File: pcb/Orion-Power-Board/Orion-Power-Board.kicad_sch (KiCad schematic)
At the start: 12 parts, among them M1 Motor_Servo, M10 Motor_Servo, M11 Motor_Servo, M12 Motor_Servo, M2 Motor_Servo, M3 Motor_Servo, M4 Motor_Servo, M5 Motor_Servo, M6 Motor_Servo, M7 Motor_Servo, M8 Motor_Servo, M9 Motor_Servo

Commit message: Power board
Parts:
- added BT1, BT2: LI-ION 7.4V 3000 mAh, AA_Custom_Components:PowerPad_Pair_5.0x5.0mm_1PadFlipped, symbol Device:Battery_Cell
- added C1, C2, C3, C4: 470uF_CAP, symbol Device:C_Polarized_US
- added C5, C6, C7, C8: 470uF_CAP, Capacitor_THT:CP_Radial_D8.0mm_P3.50mm, symbol Device:C_Polarized_US
- added H1, H2, H3, H4: MountingHole, MountingHole:MountingHole_3.2mm_M3_Pad, symbol Mechanical:MountingHole
- added J1: Keyed Connector 20 pos, AA_Custom_Components:SULLINS_SFH11-PBPC-D10-ST-BK, symbol AA_Custom_Components:20PosKeyedMale
- added J2, J3: 2S_BATTERY_BALANCE_HEADER, AA_Custom_Components:JST_XH_1x03_P2.54mm_Vertical, symbol AA_Custom_Components:2S_BATTERY_BALANCE_HEADER
- added J4: 3S_BATTERY_BALANCE_HEADER, AA_Custom_Components:JST_XH_1x04_P2.54mm_Vertical, symbol AA_Custom_Components:3S_BATTERY_BALANCE_HEADER
- added N1, N2, N4: CENTER_POS, AA_Custom_Components:Polarity_Center_Positive_7.5mm_SilkScreen, symbol Mechanical:Housing
- added N3: KiCad, Symbol:KiCad-Logo2_8mm_SilkScreen, symbol Mechanical:Housing
- added U1, U2: 6x3_SERVO_HEADER_PIN, AA_Custom_Components:PinHeader_3x06_P2.54mm_Vertical, symbol AA_Custom_Components:6x3_SERVO_HEADER_PIN
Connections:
- net +7.4V_BACK_BATT: now also BT2.1 (+), C3.1, C4.1, C7.2, C8.2, U1.1 (7.4V), U1.2 (7.4V), U1.3 (7.4V), U1.4 (7.4V), U1.5 (7.4V), U1.6 (7.4V)
- net +7.4V_FRONT_BATT: now also BT1.1 (+), C1.1, C2.1, C5.2, C6.2, U2.1 (7.4V), U2.2 (7.4V), U2.3 (7.4V), U2.4 (7.4V), U2.5 (7.4V), U2.6 (7.4V)
- net GND: now also BT1.2 (-), BT2.2 (-), C1.2, C2.2, C3.2, C4.2, C5.1, C6.1, C7.1, C8.1, J1.19, J2.3 (GND), J3.3 (GND), J4.4 (GND), U1.10 (GND), U1.11 (GND), U1.12 (GND), U1.7 (GND), U1.8 (GND), U1.9 (GND), U2.10 (GND), U2.11 (GND), U2.12 (GND), U2.7 (GND), U2.8 (GND), U2.9 (GND); no longer M9.3 (-)
- net SERVO_01: no longer names the net of M1.1 (PWM)
- net SERVO_02: no longer names the net of M3.1 (PWM)
- net SERVO_03 renamed PWM2
- net PWM2: now also J1.3, U2.16 (OUT3)
- net SERVO_04 renamed PWM3
- net PWM3: now also J1.4, U2.15 (OUT4)
- net SERVO_05 renamed PWM4
- net PWM4: now also J1.5, U2.14 (OUT5)
- net SERVO_06 renamed PWM5
- net PWM5: now also J1.6, U2.13 (OUT6)
- net SERVO_07 renamed PWM6
- net PWM6: now also J1.7, U1.18 (OUT1)
- net SERVO_08 renamed PWM7
- net PWM7: now also J1.8, U1.17 (OUT2)
- net SERVO_09 renamed PWM8
- net PWM8: now also J1.9, U1.16 (OUT3)
- net SERVO_10 renamed PWM9
- net PWM9: now also J1.10, U1.15 (OUT4)
- net SERVO_11 renamed PWM10
- net PWM10: now also J1.11, U1.14 (OUT5)
- net SERVO_12 renamed PWM11
- net PWM11: now also J1.12, U1.13 (OUT6)
- new net 2S_BACK_BATT_CELL1: J1.14, J3.1 (C1)
- new net 2S_BACK_BATT_CELL2: J1.16, J3.2 (C2)
- new net 2S_FRONT_BATT_CELL1: J1.18, J2.1 (C1)
- new net 2S_FRONT_BATT_CELL2: J1.20, J2.2 (C2)
- new net 3S_BATT_CELL1: J1.13, J4.1 (C1)
- new net 3S_BATT_CELL2: J1.15, J4.2 (C2)
- new net 3S_BATT_CELL3: J1.17, J4.3 (C3)
- new net PWM0: J1.1, U2.18 (OUT1)
- new net PWM1: J1.2, U2.17 (OUT2)
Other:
- note added: "MOUNTING HARDWARE"
- note added: "ORION POWER BOARD"
- note added: "PCB LOGOS"
- moved on the sheet: M1, M10, M11, M12, M2, M3, M4, M5, M6, M7, M8, M9

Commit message: Done layout of power board
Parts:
- removed C1, C2, C3, C4: 470uF_CAP, symbol Device:C_Polarized_US
- removed J1: Keyed Connector 20 pos, AA_Custom_Components:SULLINS_SFH11-PBPC-D10-ST-BK, symbol AA_Custom_Components:20PosKeyedMale
- removed M1, M10, M11, M12, M2, M3, M4, M5, M6, M7, M8, M9: Motor_Servo, symbol Motor:Motor_Servo
- removed N2, N4: CENTER_POS, AA_Custom_Components:Polarity_Center_Positive_7.5mm_SilkScreen, symbol Mechanical:Housing
- removed N3: KiCad, Symbol:KiCad-Logo2_8mm_SilkScreen, symbol Mechanical:Housing
- added J5: 3S_LI-ION_VOLTAGE_ALARM, AA_Custom_Components:LIPO_VOLTAGE_ALARM, symbol AA_Custom_Components:LIPO_VOLTAGE_ALARM
- added J6: 2S_BACK_LI-ION_VOLTAGE_ALARM, AA_Custom_Components:LIPO_VOLTAGE_ALARM, symbol AA_Custom_Components:LIPO_VOLTAGE_ALARM
- added J7: 2S_FRONT_LI-ION_VOLTAGE_ALARM, AA_Custom_Components:LIPO_VOLTAGE_ALARM, symbol AA_Custom_Components:LIPO_VOLTAGE_ALARM
- added J8: CONN_20_POS_KEYED_SOCKET, AA_Custom_Components:SULLINS_SBH11-PBPC-D10-ST-BK_SOCKET, symbol AA_Custom_Components:CONN_20_POS_KEYED_SOCKET
- BT1: value LI-ION 7.4V 3000 mAh -> 2S_FRONT_LI-ION_BATT; footprint AA_Custom_Components:PowerPad_Pair_5.0x5.0mm_1PadFlipped -> AA_Custom_Components:PowerPad_Pair_5.0x5.0mm_2ndPadFlipped
- BT2: value LI-ION 7.4V 3000 mAh -> 2S_BACK_LI-ION_BATT; footprint AA_Custom_Components:PowerPad_Pair_5.0x5.0mm_1PadFlipped -> AA_Custom_Components:PowerPad_Pair_5.0x5.0mm_2ndPadFlipped
- J2: value 2S_BATTERY_BALANCE_HEADER -> 2S_FRONT_BATTERY_BALANCE_HEADER
- J3: value 2S_BATTERY_BALANCE_HEADER -> 2S_BACK_BATTERY_BALANCE_HEADER
- U1: value 6x3_SERVO_HEADER_PIN -> BACK_6x3_SERVO_HEADER_PIN; footprint AA_Custom_Components:PinHeader_3x06_P2.54mm_Vertical -> AA_Custom_Components:Servo_PinHeader_3x06_P2.54mm_Vertical
- U2: value 6x3_SERVO_HEADER_PIN -> FRONT_6x3_SERVO_HEADER_PIN; footprint AA_Custom_Components:PinHeader_3x06_P2.54mm_Vertical -> AA_Custom_Components:Servo_PinHeader_3x06_P2.54mm_Vertical
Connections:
- net +7.4V_BACK_BATT: now also U1.10 (7.4V), U1.11 (7.4V), U1.12 (7.4V), U1.7 (7.4V), U1.8 (7.4V), U1.9 (7.4V); no longer U1.1 (7.4V), U1.2 (7.4V), U1.3 (7.4V), U1.4 (7.4V), U1.5 (7.4V), U1.6 (7.4V)
- net +7.4V_FRONT_BATT: now also U2.10 (7.4V), U2.11 (7.4V), U2.12 (7.4V), U2.7 (7.4V), U2.8 (7.4V), U2.9 (7.4V); no longer U2.1 (7.4V), U2.2 (7.4V), U2.3 (7.4V), U2.4 (7.4V), U2.5 (7.4V), U2.6 (7.4V)
- net 3S_BATT_CELL1: now also J5.2 (1S), J8.13
- net 3S_BATT_CELL2: now also J5.3 (2S), J8.15
- net 3S_BATT_CELL3: now also J5.4 (3S), J8.17
- net GND: now also U1.13 (GND), U1.14 (GND), U1.15 (GND), U1.16 (GND), U1.17 (GND), U1.18 (GND), U2.13 (GND), U2.14 (GND), U2.15 (GND), U2.16 (GND), U2.17 (GND), U2.18 (GND), J5.1 (GND), J6.1 (GND), J7.1 (GND), J8.19; no longer U1.10 (GND), U1.11 (GND), U1.12 (GND), U1.7 (GND), U1.8 (GND), U1.9 (GND), U2.10 (GND), U2.11 (GND), U2.12 (GND), U2.7 (GND), U2.8 (GND), U2.9 (GND)
- net PWM0: now also U2.1 (PWM0), J8.1; no longer U2.18 (OUT1)
- net PWM1: now also U2.2 (PWM1), J8.2; no longer U2.17 (OUT2)
- net PWM10: now also U1.5 (PWM4), J8.11; no longer U1.14 (OUT5)
- net PWM11: now also U1.6 (PWM5), J8.12; no longer U1.13 (OUT6)
- net PWM2: now also U2.3 (PWM2), J8.3; no longer U2.16 (OUT3)
- net PWM3: now also U2.4 (PWM3), J8.4; no longer U2.15 (OUT4)
- net PWM4: now also U2.5 (PWM4), J8.5; no longer U2.14 (OUT5)
- net PWM5: now also U2.6 (PWM5), J8.6; no longer U2.13 (OUT6)
- net PWM6: now also U1.1 (PWM0), J8.7; no longer U1.18 (OUT1)
- net PWM7: now also U1.2 (PWM1), J8.8; no longer U1.17 (OUT2)
- net PWM8: now also U1.3 (PWM2), J8.9; no longer U1.16 (OUT3)
- net PWM9: now also U1.4 (PWM3), J8.10; no longer U1.15 (OUT4)
- net 2S_BACK_BATT_CELL1 renamed 2S_BATT_REAR_CELL1
- net 2S_BATT_REAR_CELL1: now also J6.2 (1S), J8.14
- net 2S_BACK_BATT_CELL2 renamed 2S_BATT_REAR_CELL2
- net 2S_BATT_REAR_CELL2: now also J6.3 (2S), J8.16
- net 2S_FRONT_BATT_CELL1 renamed 2S_BATT_FRONT_CELL1
- net 2S_BATT_FRONT_CELL1: now also J7.2 (1S), J8.18
- net 2S_FRONT_BATT_CELL2 renamed 2S_BATT_FRONT_CELL2
- net 2S_BATT_FRONT_CELL2: now also J7.3 (2S), J8.20
- no-connect marks 0 -> 17
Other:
- moved on the sheet: BT1, BT2, C5, C6, C7, C8, N1

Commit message: Update power board
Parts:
- N1: value CENTER_POS -> ORION_LOGO; footprint AA_Custom_Components:Polarity_Center_Positive_7.5mm_SilkScreen -> Orion-Logo:Orion-Logo-20mm
- renumbered C6 to C1, C7 to C2, C5 to C3, C8 to C4, J2 to J1, J3 to J2, J4 to J3, J8 to J4, J7 to J5, J5 to J7, U2 to U1, U1 to U2
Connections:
- net 2S_BATT_FRONT_CELL1: now also J4.16; no longer J4.18
- net 2S_BATT_FRONT_CELL2: now also J4.14; no longer J4.20
- net 2S_BATT_REAR_CELL1: now also J4.20; no longer J4.14
- net 2S_BATT_REAR_CELL2: now also J4.18; no longer J4.16
- net 3S_BATT_CELL1: now also J4.17; no longer J4.13
- net 3S_BATT_CELL3: now also J4.13; no longer J4.17

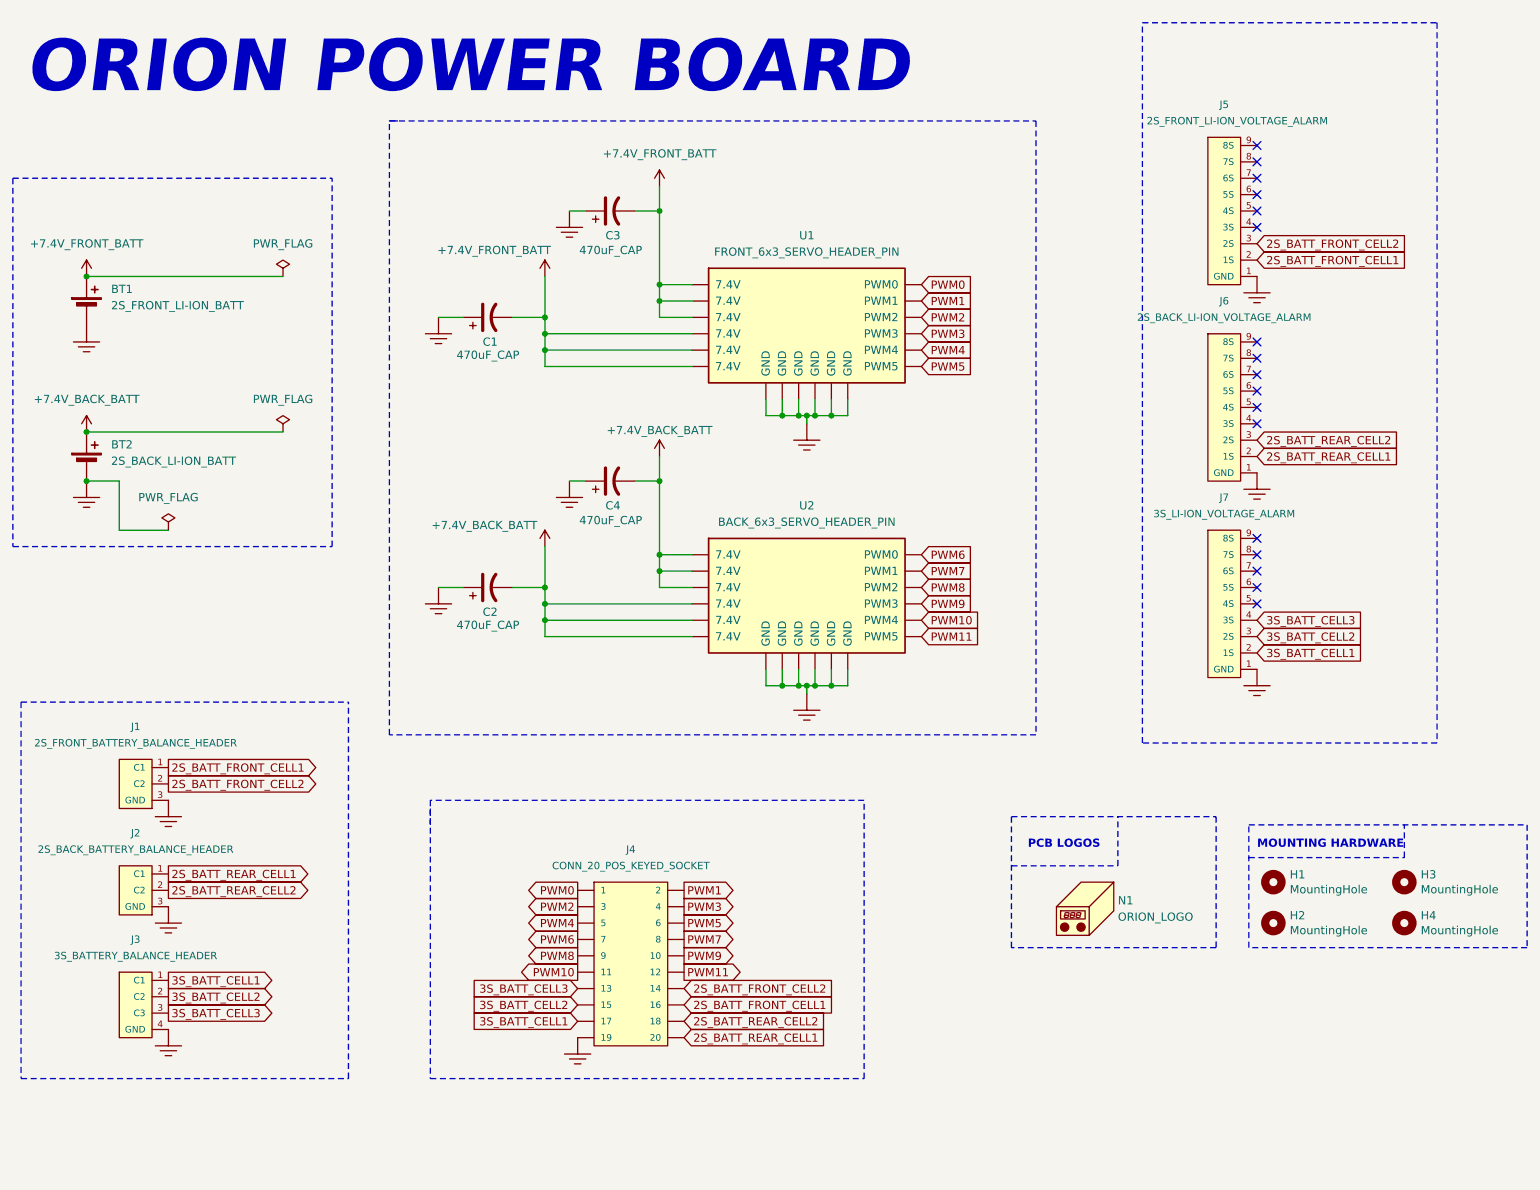
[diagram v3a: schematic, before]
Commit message: Almost finished power board
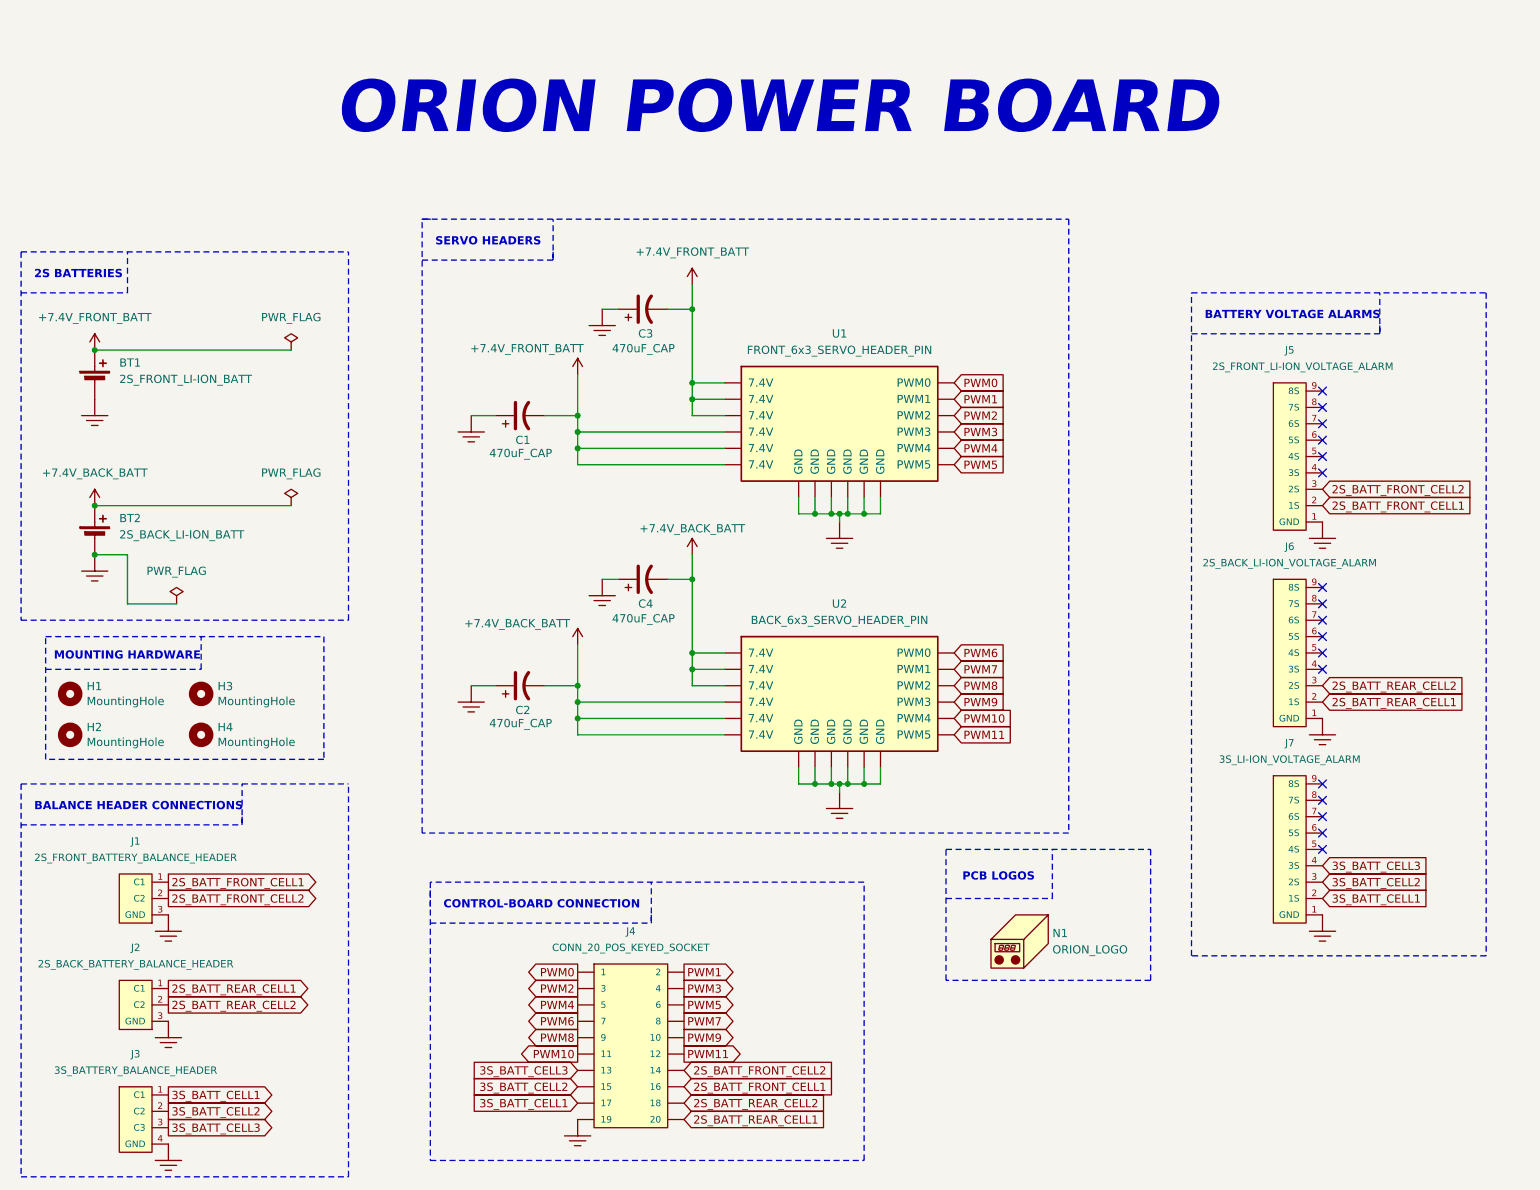
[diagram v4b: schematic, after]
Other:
- note added: "2S BATTERIES"
- note added: "BALANCE HEADER CONNECTIONS"
- note added: "BATTERY VOLTAGE ALARMS"
- note added: "CONTROL-BOARD CONNECTION"
- note added: "SERVO HEADERS"
- moved on the sheet: BT1, BT2, C1, C2, C3, C4, H1, H2, H3, H4, J1, J2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

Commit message: Finished power board
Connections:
- net +7.4V_FRONT_BATT: now also C1.1, C3.1; no longer C1.2, C3.2
- net 2S_BATT_FRONT_CELL1: now also J1.2 (C1); no longer J1.1 (C1)
- net 2S_BATT_FRONT_CELL2: now also J1.1 (C2); no longer J1.2 (C2)
- net 2S_BATT_REAR_CELL1: now also J2.2 (C1); no longer J2.1 (C1)
- net 2S_BATT_REAR_CELL2: now also J2.1 (C2); no longer J2.2 (C2)
- net 3S_BATT_CELL1: now also J3.3 (C1); no longer J3.1 (C1)
- net 3S_BATT_CELL3: now also J3.1 (C3); no longer J3.3 (C3)
- net GND: now also C1.2, C2.2, C3.2, C4.2; no longer C1.1, C2.1, C3.1, C4.1
- net +7.4V_BACK_BATT renamed +7.4V_REAR_BATT
- net +7.4V_REAR_BATT: now also C2.1, C4.1; no longer C2.2, C4.2
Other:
- moved on the sheet: C1, C2, C3, C4
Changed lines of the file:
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@@
 		)
 	)
-	(global_label "2S_BATT_FRONT_CELL1"
+	(global_label "2S_BATT_FRONT_CELL2"
 		(shape output)
 		(at 44.45 154.94 0)
@@
 		)
 	)
-	(global_label "2S_BATT_REAR_CELL1"
+	(global_label "2S_BATT_REAR_CELL2"
 		(shape output)
 		(at 44.45 171.45 0)
@@
 		)
 	)
-	(global_label "2S_BATT_REAR_CELL2"
+	(global_label "2S_BATT_REAR_CELL1"
 		(shape output)
 		(at 44.45 173.99 0)
@@
 		)
 	)
-	(global_label "2S_BATT_FRONT_CELL2"
+	(global_label "2S_BATT_FRONT_CELL1"
 		(shape output)
 		(at 44.45 157.48 0)
@@
 		)
 	)
-	(global_label "3S_BATT_CELL1"
+	(global_label "3S_BATT_CELL3"
 		(shape output)
 		(at 44.45 187.96 0)
@@
 		)
 	)
-	(global_label "3S_BATT_CELL3"
+	(global_label "3S_BATT_CELL1"
 		(shape output)
 		(at 44.45 193.04 0)
@@
 	(symbol
 		(lib_id "Device:C_Polarized_US")
-		(at 118.11 66.04 90)
+		(at 118.11 66.04 270)
 		(unit 1)
 		(exclude_from_sim no)
@@
 		(dnp no)
 		(property "Reference" "C3"
-			(at 117.348 69.85 90)
+			(at 118.872 62.23 90)
 			(effects
 				(font
@@
 		)
 		(property "Value" "470uF_CAP"
-			(at 113.284 72.136 90)
+			(at 124.968 69.342 90)
 			(effects
 				(font
@@
 			)
 		)
-		(property "Value" "+7.4V_BACK_BATT"
+		(property "Value" "+7.4V_REAR_BATT"
 			(at 33.02 91.44 0)
 			(effects
@@
 	(symbol
 		(lib_id "Device:C_Polarized_US")
-		(at 99.06 82.55 90)
+		(at 99.06 82.55 270)
 		(unit 1)
 		(exclude_from_sim no)
@@
 		(dnp no)
 		(property "Reference" "C1"
-			(at 98.298 86.36 90)
+			(at 100.076 78.994 90)
 			(effects
 				(font
@@
 		)
 		(property "Value" "470uF_CAP"
-			(at 94.234 88.392 90)
+			(at 105.156 85.852 90)
 			(effects
 				(font
@@
 			)
 		)
-		(property "Value" "+7.4V_BACK_BATT"
+		(property "Value" "+7.4V_REAR_BATT"
 			(at 98.552 114.808 0)
 			(effects
@@
 	(symbol
 		(lib_id "Device:C_Polarized_US")
-		(at 99.06 124.46 90)
+		(at 99.06 124.46 270)
 		(unit 1)
 		(exclude_from_sim no)
@@
 		(dnp no)
 		(property "Reference" "C2"
-			(at 98.298 128.27 90)
+			(at 97.536 123.19 90)
 			(effects
 				(font
@@
 		)
 		(property "Value" "470uF_CAP"
-			(at 94.234 130.302 90)
+			(at 105.41 127.762 90)
 			(effects
 				(font
@@
 	)
 	(symbol
-		(lib_name "2S_BATTERY_BALANCE_HEADER_1")
 		(lib_id "AA_Custom_Components:2S_BATTERY_BALANCE_HEADER")
 		(at 41.91 160.02 0)
@@
 	(symbol
 		(lib_id "Device:C_Polarized_US")
-		(at 118.11 107.95 90)
+		(at 118.11 107.95 270)
 		(unit 1)
 		(exclude_from_sim no)
@@
 		(dnp no)
 		(property "Reference" "C4"
-			(at 117.348 111.76 90)
+			(at 118.872 104.394 90)
 			(effects
 				(font
@@
 		)
 		(property "Value" "470uF_CAP"
-			(at 113.284 114.046 90)
+			(at 124.714 111.252 90)
 			(effects
 				(font
@@
 			)
 		)
-		(property "Value" "+7.4V_BACK_BATT"
+		(property "Value" "+7.4V_REAR_BATT"
 			(at 125.73 100.076 0)
 			(effects

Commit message: Update schematics
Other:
- note added: "POWER BOARD"
- note removed: "ORION POWER BOARD"
- moved on the sheet: C1, C2, C3, C4, U1, U2
